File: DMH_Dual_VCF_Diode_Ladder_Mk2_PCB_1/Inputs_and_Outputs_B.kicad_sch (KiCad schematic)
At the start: 8 parts, among them J10 TS_Jack_6.35mm_Sw, J210 IDC_02x05, J6 TS_Jack_6.35mm_Sw, J7 TS_Jack_6.35mm_Sw, J70 Conn_01x06, J8 TS_Jack_6.35mm_Sw, J80 Conn_01x06, J9 TS_Jack_6.35mm_Sw

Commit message: Added CV3 and Drive CV to I/O pages
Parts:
- removed J70, J80: Conn_01x06, Connector_PinSocket_2.54mm:PinSocket_1x06_P2.54mm_Vertical, symbol Connector_Generic:Conn_01x06
- added J13, J14: TS_Jack_6.35mm_Sw, SynthStuff:CUI_MJ-63052A, symbol SynthStuff:TS_Jack_6.35mm_Sw
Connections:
- net GND: now also J13.S, J14.S; no longer J210.4 (Pin_4), J210.9 (Pin_9)
- net Res CV TN: now also J210.7 (Pin_7); no longer J210.6 (Pin_6)
- net at J10.TN: now also J210.8 (Pin_8); no longer J210.7 (Pin_7)
- new net CV 3 Jack: J13.T
- new net CV3 TN: J13.TN, J210.4 (Pin_4)
- new net Drive CV Jack: J14.T
- new net Drive CV TN: J14.TN, J210.6 (Pin_6)
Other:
- note removed: "Connectors PCB"
- moved on the sheet: J10, J210, J9

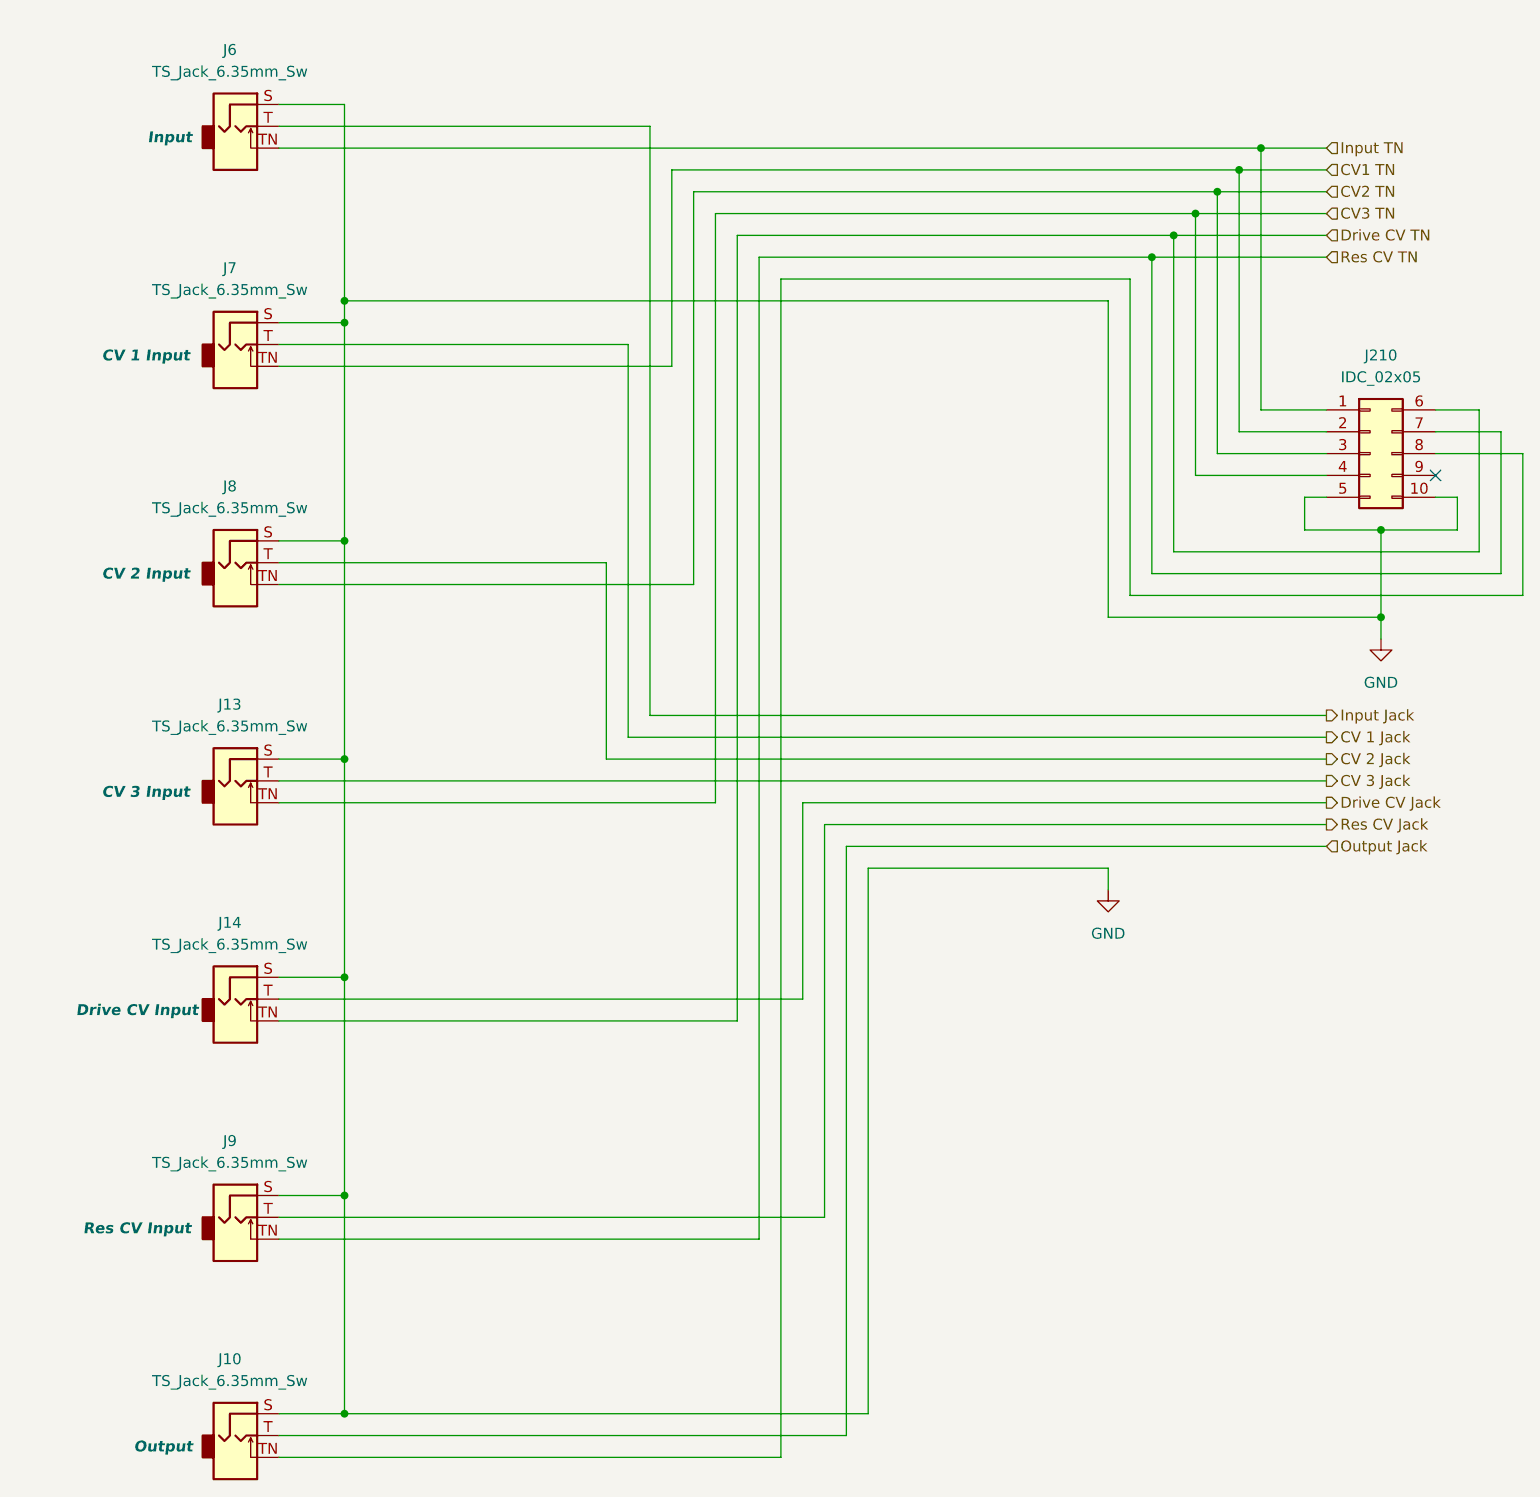
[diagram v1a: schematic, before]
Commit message: Added board-to-board pins to schematic
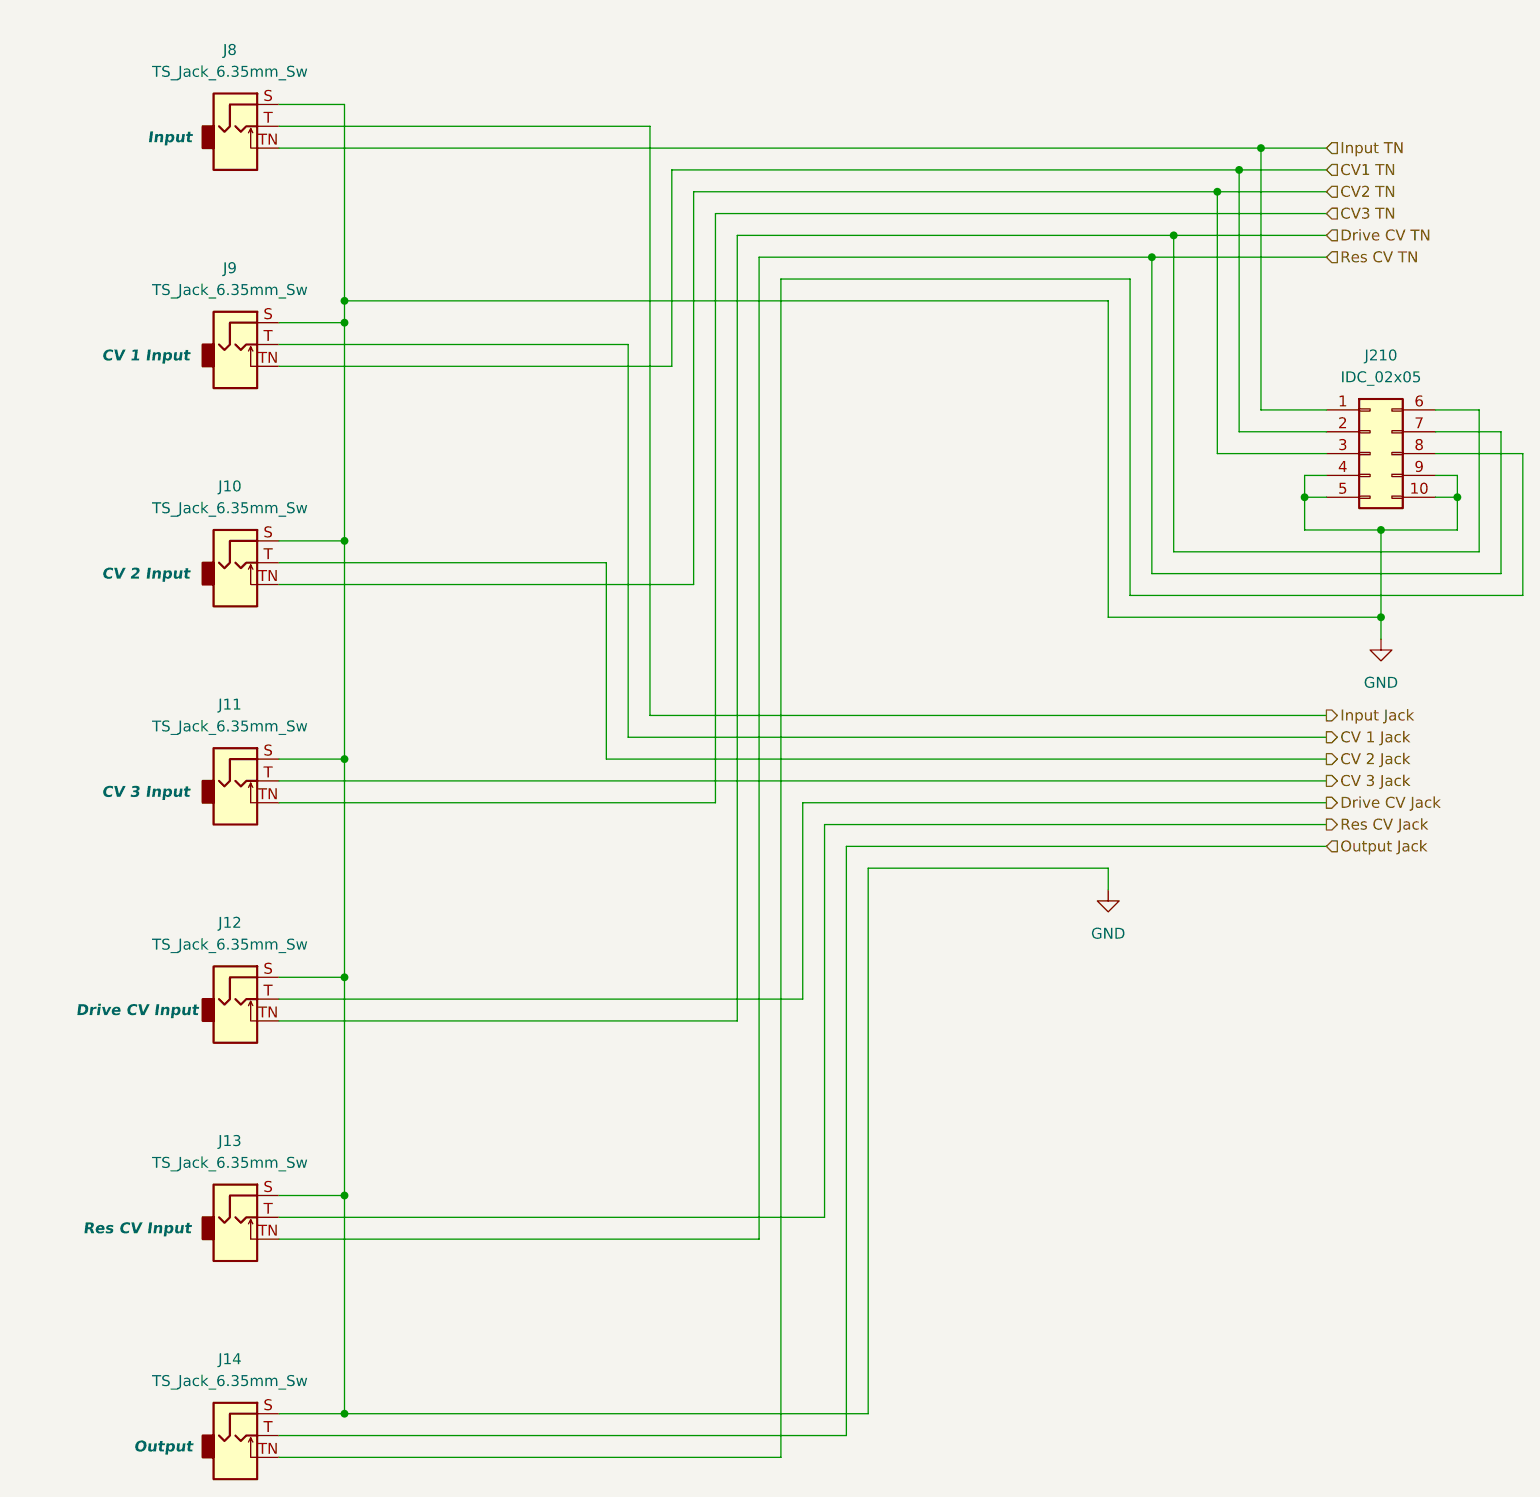
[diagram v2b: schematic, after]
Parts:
- renumbered J8 to J10, J13 to J11, J14 to J12, J9 to J13, J10 to J14, J6 to J8, J7 to J9
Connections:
- net CV3 TN: no longer J210.4 (Pin_4)
- net GND: now also J210.4 (Pin_4), J210.9 (Pin_9)
- no-connect marks 1 -> 0
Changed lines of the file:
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@@
+	)
+	(junction
+		(at 175.26 81.28)
+		(diameter 0)
+		(color 0 0 0 0)
 	)
 	(junction
@@
 	)
 	(junction
+		(at 193.04 81.28)
+		(diameter 0)
+		(color 0 0 0 0)
+	)
+	(junction
 		(at 63.5 86.36)
 		(diameter 0)
@@
 	)
 	(junction
-		(at 162.56 48.26)
-		(diameter 0)
-		(color 0 0 0 0)
-	)
-	(junction
 		(at 63.5 60.96)
 		(diameter 0)
 		(color 0 0 0 0)
 	)
-	(no_connect
-		(at 190.5 78.74)
-	)
 	(wire
 		(pts
@@
 	(wire
 		(pts
+			(xy 190.5 78.74) (xy 193.04 78.74)
+		)
+		(stroke
+			(width 0)
+			(type default)
+		)
+	)
+	(wire
+		(pts
 			(xy 99.06 38.1) (xy 99.06 106.68)
 		)
@@
 	(wire
 		(pts
-			(xy 162.56 48.26) (xy 162.56 78.74)
+			(xy 177.8 78.74) (xy 175.26 78.74)
 		)
 		(stroke
@@
 	(wire
 		(pts
-			(xy 106.68 48.26) (xy 162.56 48.26)
-		)
-		(stroke
-			(width 0)
-			(type default)
-		)
-	)
-	(wire
-		(pts
 			(xy 111.76 167.64) (xy 111.76 53.34)
 		)
@@
 	(wire
 		(pts
+			(xy 193.04 78.74) (xy 193.04 81.28)
+		)
+		(stroke
+			(width 0)
+			(type default)
+		)
+	)
+	(wire
+		(pts
 			(xy 165.1 45.72) (xy 177.8 45.72)
 		)
@@
 	(wire
 		(pts
+			(xy 175.26 78.74) (xy 175.26 81.28)
+		)
+		(stroke
+			(width 0)
+			(type default)
+		)
+	)
+	(wire
+		(pts
 			(xy 55.88 139.7) (xy 116.84 139.7)
 		)
@@
 	(wire
 		(pts
-			(xy 162.56 48.26) (xy 177.8 48.26)
+			(xy 106.68 48.26) (xy 177.8 48.26)
 		)
 		(stroke
@@
 		(pts
 			(xy 121.92 121.92) (xy 177.8 121.92)
-		)
-		(stroke
-			(width 0)
-			(type default)
-		)
-	)
-	(wire
-		(pts
-			(xy 162.56 78.74) (xy 177.8 78.74)
 		)
 		(stroke
@@
 		(on_board no)
 		(dnp no)
-		(property "Reference" "J8"
+		(property "Reference" "J10"
 			(at 50.165 80.01 0)
 			(effects
@@
 			(project "DMH_Dual_VCF_Diode_Ladder_PCB"
 				(path "/58f4306d-5387-4983-bb08-41a2313fd315/f24a7deb-7368-4909-ac96-a87cdb4f6b04"
-					(reference "J8")
+					(reference "J10")
 					(unit 1)
 				)
@@
 		(on_board no)
 		(dnp no)
-		(property "Reference" "J14"
+		(property "Reference" "J12"
 			(at 50.165 130.81 0)
 			(effects
@@
 			(project "DMH_Dual_VCF_Diode_Ladder_Mk2_PCB_1"
 				(path "/58f4306d-5387-4983-bb08-41a2313fd315/f24a7deb-7368-4909-ac96-a87cdb4f6b04"
-					(reference "J14")
+					(reference "J12")
 					(unit 1)
 				)
@@
 		(on_board no)
 		(dnp no)
-		(property "Reference" "J10"
+		(property "Reference" "J14"
 			(at 50.165 181.61 0)
 			(effects
@@
 			(project "DMH_Dual_VCF_Diode_Ladder_PCB"
 				(path "/58f4306d-5387-4983-bb08-41a2313fd315/f24a7deb-7368-4909-ac96-a87cdb4f6b04"
-					(reference "J10")
+					(reference "J14")
 					(unit 1)
 				)
@@
 		(on_board no)
 		(dnp no)
-		(property "Reference" "J7"
+		(property "Reference" "J9"
 			(at 50.165 54.61 0)
 			(effects
@@
 			(project "DMH_Dual_VCF_Diode_Ladder_PCB"
 				(path "/58f4306d-5387-4983-bb08-41a2313fd315/f24a7deb-7368-4909-ac96-a87cdb4f6b04"
-					(reference "J7")
+					(reference "J9")
 					(unit 1)
 				)
@@
 		(on_board no)
 		(dnp no)
-		(property "Reference" "J6"
+		(property "Reference" "J8"
 			(at 50.165 29.21 0)
 			(effects
@@
 			(project "DMH_Dual_VCF_Diode_Ladder_PCB"
 				(path "/58f4306d-5387-4983-bb08-41a2313fd315/f24a7deb-7368-4909-ac96-a87cdb4f6b04"
-					(reference "J6")
+					(reference "J8")
 					(unit 1)
 				)
@@
 		(on_board no)
 		(dnp no)
-		(property "Reference" "J13"
+		(property "Reference" "J11"
 			(at 50.165 105.41 0)
 			(effects
@@
 			(project "DMH_Dual_VCF_Diode_Ladder_Mk2_PCB_1"
 				(path "/58f4306d-5387-4983-bb08-41a2313fd315/f24a7deb-7368-4909-ac96-a87cdb4f6b04"
-					(reference "J13")
+					(reference "J11")
 					(unit 1)
 				)
@@
 		(on_board no)
 		(dnp no)
-		(property "Reference" "J9"
+		(property "Reference" "J13"
 			(at 50.165 156.21 0)
 			(effects
@@
 			(project "DMH_Dual_VCF_Diode_Ladder_PCB"
 				(path "/58f4306d-5387-4983-bb08-41a2313fd315/f24a7deb-7368-4909-ac96-a87cdb4f6b04"
-					(reference "J9")
+					(reference "J13")
 					(unit 1)
 				)
